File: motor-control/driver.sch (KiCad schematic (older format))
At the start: 25 parts, among them U4 DRV8301

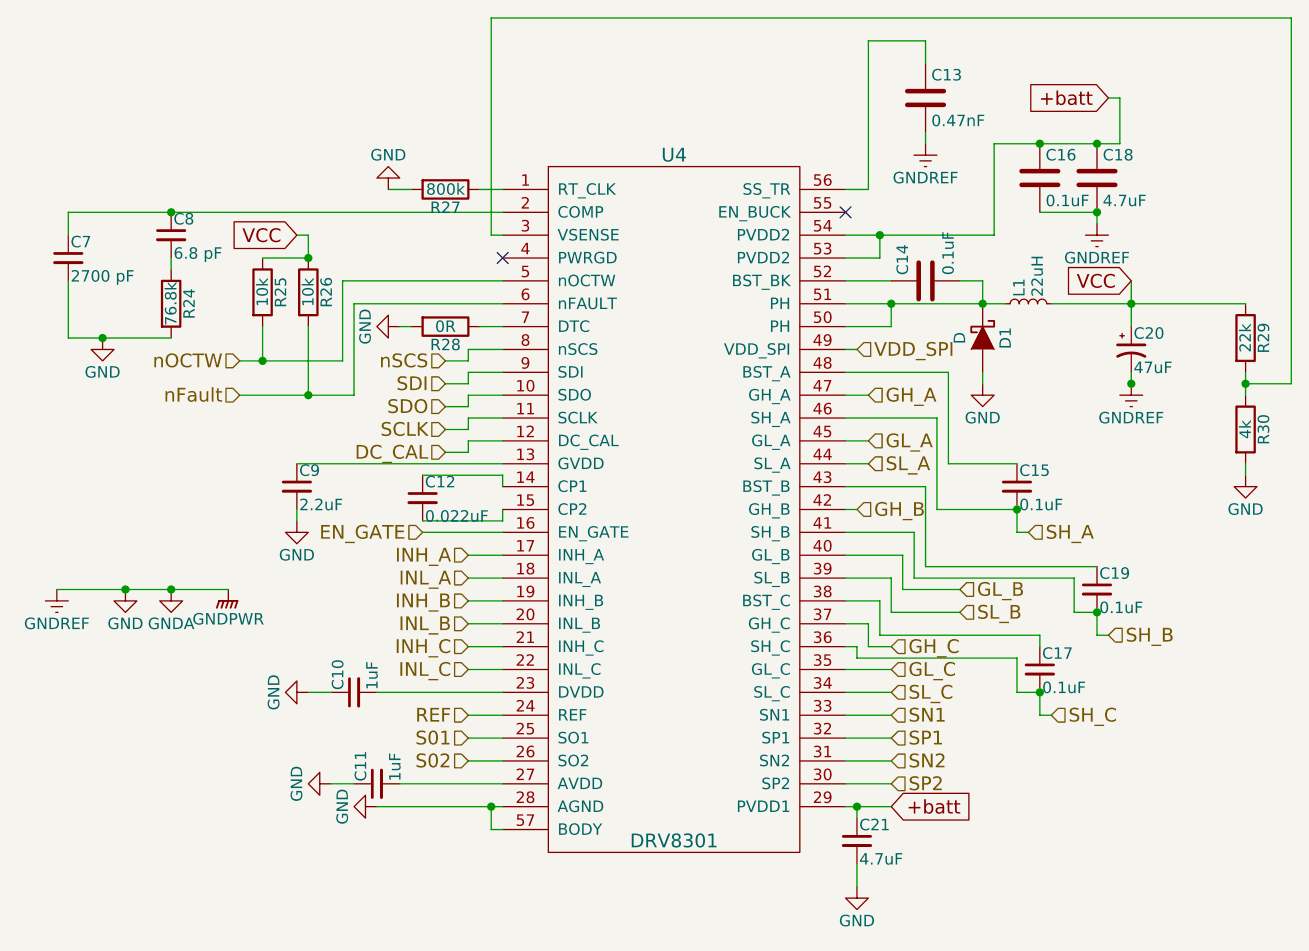
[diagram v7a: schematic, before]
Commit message: Chnaged schematic buck values according to TI
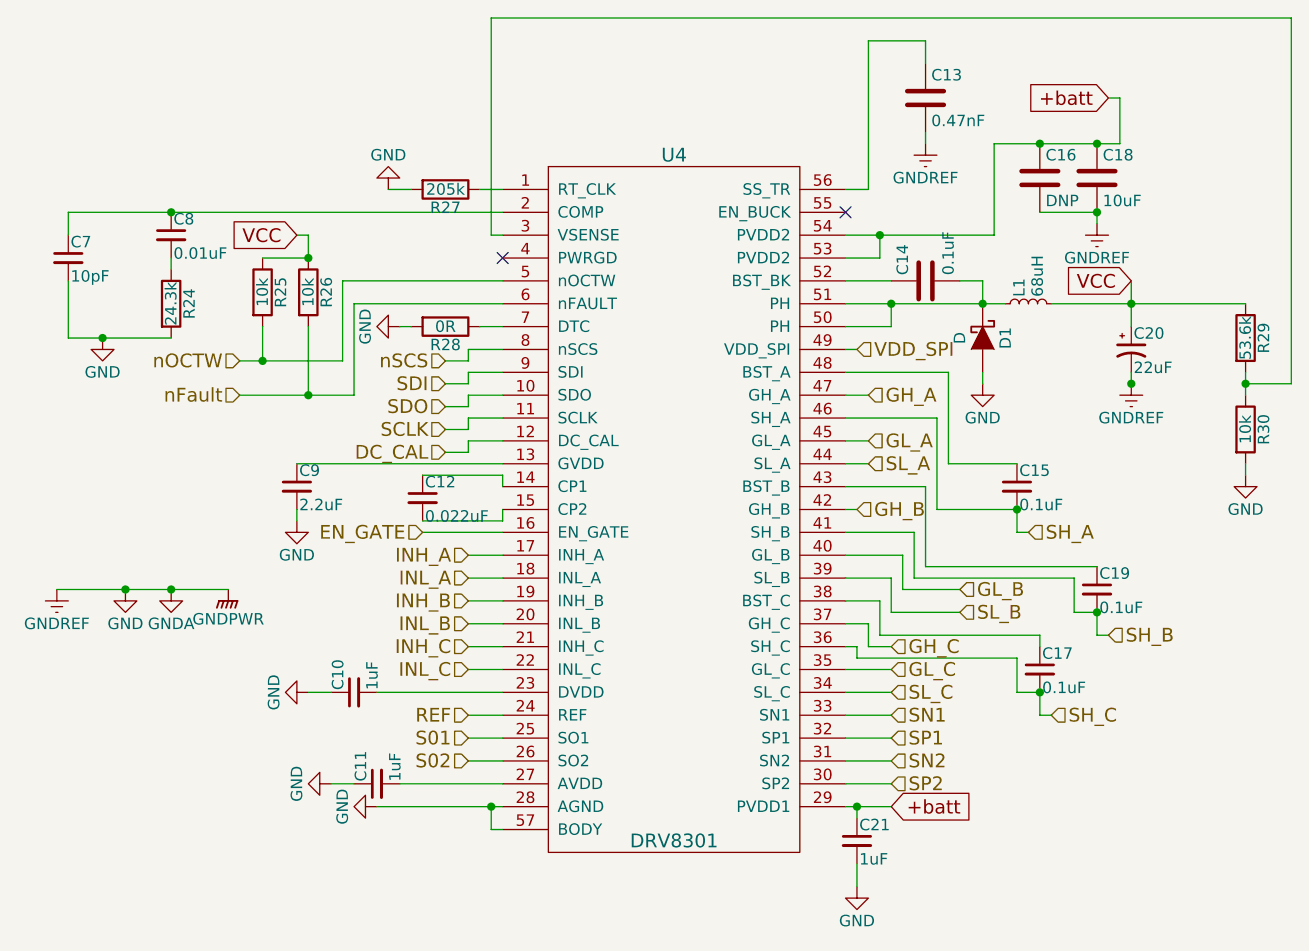
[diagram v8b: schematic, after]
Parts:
- C16: value 0.1uF -> DNP
- C18: value 4.7uF -> 10uF
- C20: value 47uF -> 22uF
- C21: value 4.7uF -> 1uF
- C7: value 2700 pF -> 10pF
- C8: value 6.8 pF -> 0.01uF
- D1: footprint Diodes_ThroughHole:Diode_TO-247_Vertical -> p16261:B220A-13-F
- L1: value 22uH -> 68uH; footprint Inductors:INDUCTOR_V -> p16261:inductor_custom
- R24: value 76.8k -> 24.3k
- R27: value 800k -> 205k
- R29: value 22k -> 53.6k
- R30: value 4k -> 10k
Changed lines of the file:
@@
 LIBS:contrib
 LIBS:valves
-LIBS:p16261
-LIBS:my_lib
 LIBS:_saved_motor-control-cache
 EELAYER 25 0
@@
 P 6500 1900
 F 0 "C16" H 6525 2000 50  0000 L CNN
-F 1 "0.1uF" H 6525 1800 50  0000 L CNN
+F 1 "DNP" H 6525 1800 50  0000 L CNN
 F 2 "Capacitors_SMD:C_0805" H 6538 1750 30  0001 C CNN
 F 3 "" H 6500 1900 60  0000 C CNN
@@
 P 6750 1900
 F 0 "C18" H 6775 2000 50  0000 L CNN
-F 1 "4.7uF" H 6775 1800 50  0000 L CNN
+F 1 "10uF" H 6775 1800 50  0000 L CNN
 F 2 "Capacitors_SMD:C_0805" H 6788 1750 30  0001 C CNN
 F 3 "" H 6750 1900 60  0000 C CNN
@@
 P 6450 2450
 F 0 "L1" H 6480 2490 50  0000 L CNN
-F 1 "22uH" H 6480 2410 50  0000 L CNN
-F 2 "Inductors:INDUCTOR_V" H 6450 2450 60  0001 C CNN
-F 3 "" H 6450 2450 60  0000 C CNN
+F 1 "68uH" H 6480 2410 50  0000 L CNN
+F 2 "p16261:inductor_custom" H 6450 2450 60  0001 C CNN
+F 3 "http://www.coilcraft.com/pdfs/pch.pdf" H 6450 2450 60  0001 C CNN
 	1    6450 2450
 	0    -1   -1   0
@@
 F 0 "D1" H 6250 2700 50  0000 C CNN
 F 1 "D" H 6250 2500 50  0000 C CNN
-F 2 "Diodes_ThroughHole:Diode_TO-247_Vertical" H 6250 2600 60  0001 C CNN
-F 3 "" H 6250 2600 60  0000 C CNN
+F 2 "p16261:B220A-13-F" H 6250 2600 60  0001 C CNN
+F 3 "http://www.mouser.com/Search/ProductDetail.aspx?R=B220A-13-Fvirtualkey62110000virtualkey621-B220A-F" H 6250 2600 60  0001 C CNN
 	1    6250 2600
 	0    1    1    0
@@
 P 6900 2650
 F 0 "C20" H 6910 2720 50  0000 L CNN
-F 1 "47uF" H 6910 2570 50  0000 L CNN
+F 1 "22uF" H 6910 2570 50  0000 L CNN
 F 2 "Capacitors_SMD:C_0805" H 6900 2650 60  0001 C CNN
 F 3 "" H 6900 2650 60  0000 C CNN
@@
 P 2250 2250
 F 0 "C7" H 2260 2320 50  0000 L CNN
-F 1 "2700 pF" H 2260 2170 50  0000 L CNN
+F 1 "10pF" H 2260 2170 50  0000 L CNN
 F 2 "Capacitors_SMD:C_0805" H 2250 2250 60  0001 C CNN
 F 3 "" H 2250 2250 60  0000 C CNN
@@
 P 2700 2150
 F 0 "C8" H 2710 2220 50  0000 L CNN
-F 1 "6.8 pF" H 2710 2070 50  0000 L CNN
+F 1 "0.01uF" H 2710 2070 50  0000 L CNN
 F 2 "Capacitors_SMD:C_0805" H 2700 2150 60  0001 C CNN
 F 3 "" H 2700 2150 60  0000 C CNN
@@
 P 2700 2450
 F 0 "R24" V 2780 2450 50  0000 C CNN
-F 1 "76.8k" V 2700 2450 50  0000 C CNN
+F 1 "24.3k" V 2700 2450 50  0000 C CNN
 F 2 "Resistors_SMD:R_0805" V 2630 2450 30  0001 C CNN
 F 3 "" H 2700 2450 30  0000 C CNN
@@
 P 3900 1950
 F 0 "R27" V 3980 1950 50  0000 C CNN
-F 1 "800k" V 3900 1950 50  0000 C CNN
+F 1 "205k" V 3900 1950 50  0000 C CNN
 F 2 "Resistors_SMD:R_0805" V 3830 1950 30  0001 C CNN
 F 3 "" H 3900 1950 30  0000 C CNN
@@
 P 7400 2600
 F 0 "R29" V 7480 2600 50  0000 C CNN
-F 1 "22k" V 7400 2600 50  0000 C CNN
+F 1 "53.6k" V 7400 2600 50  0000 C CNN
 F 2 "Resistors_SMD:R_0805" V 7330 2600 30  0001 C CNN
 F 3 "" H 7400 2600 30  0000 C CNN
@@
 P 7400 3000
 F 0 "R30" V 7480 3000 50  0000 C CNN
-F 1 "4k" V 7400 3000 50  0000 C CNN
+F 1 "10k" V 7400 3000 50  0000 C CNN
 F 2 "Resistors_SMD:R_0805" V 7330 3000 30  0001 C CNN
 F 3 "" H 7400 3000 30  0000 C CNN
@@
 P 5700 4800
 F 0 "C21" H 5710 4870 50  0000 L CNN
-F 1 "4.7uF" H 5710 4720 50  0000 L CNN
+F 1 "1uF" H 5710 4720 50  0000 L CNN
 F 2 "Capacitors_SMD:C_0805" H 5700 4800 50  0001 C CNN
 F 3 "" H 5700 4800 50  0000 C CNN
